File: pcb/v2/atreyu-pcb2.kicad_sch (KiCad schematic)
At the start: 126 parts, among them SW1 SW_Push, SW2 RotaryEncoder_Switch, SW3 RotaryEncoder_Switch, U1 Elite-C

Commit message: Checkpoint commit.
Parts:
- added J1: OLED, Connector_PinHeader_2.54mm:PinHeader_1x04_P2.54mm_Vertical, symbol SouffleKeyboard-rescue:OLED-Lily58-cache
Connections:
- net COL0: now also U1.26 (D5); no longer U1.8 (5/PC6)
- net COL1: now also U1.25 (B7); no longer U1.7 (4/PD4)
- net COL2: now also U1.8 (5/PC6); no longer U1.6 (3/PD0)
- net COL3: now also U1.7 (4/PD4); no longer U1.5 (2/PD1)
- net GND: now also J1.4 (P4)
- net VCC: now also J1.3 (P3)
- new net SCL: J1.2 (P2), U1.6 (3/PD0)
- new net SDA: J1.1 (P1), U1.5 (2/PD1)
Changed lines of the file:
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@@
+    )
+  )
+  (global_label "SCL" (shape input) (at 71.12 140.97 270) (fields_autoplaced)
+    (effects (font (size 1.27 1.27)) (justify right))
+    (property "Intersheet References" "${INTERSHEET_REFS}" (id 0) (at 71.0406 146.8907 90)
+      (effects (font (size 1.27 1.27)) (justify right) hide)
     )
   )
@@
     )
   )
+  (global_label "VCC" (shape input) (at 73.66 140.97 270) (fields_autoplaced)
+    (effects (font (size 1.27 1.27)) (justify right))
+    (property "Intersheet References" "${INTERSHEET_REFS}" (id 0) (at 73.5806 147.0117 90)
+      (effects (font (size 1.27 1.27)) (justify right) hide)
+    )
+  )
+  (global_label "SDA" (shape input) (at 96.52 158.75 180) (fields_autoplaced)
+    (effects (font (size 1.27 1.27)) (justify right))
+    (property "Intersheet References" "${INTERSHEET_REFS}" (id 0) (at 90.5388 158.6706 0)
+      (effects (font (size 1.27 1.27)) (justify right) hide)
+    )
+  )
   (global_label "SW54A" (shape input) (at 190.5 142.24 0) (fields_autoplaced)
     (effects (font (size 1.27 1.27)) (justify left))
@@
     )
   )
-  (global_label "COL3" (shape input) (at 96.52 158.75 180) (fields_autoplaced)
-    (effects (font (size 1.27 1.27)) (justify right))
-    (property "Intersheet References" "${INTERSHEET_REFS}" (id 0) (at 265.43 317.5 0)
+  (global_label "COL3" (shape input) (at 96.52 163.83 180) (fields_autoplaced)
+    (effects (font (size 1.27 1.27)) (justify right))
+    (property "Intersheet References" "${INTERSHEET_REFS}" (id 0) (at 265.43 322.58 0)
       (effects (font (size 1.27 1.27)) hide)
     )
@@
     )
   )
-  (global_label "COL0" (shape input) (at 96.52 166.37 180) (fields_autoplaced)
-    (effects (font (size 1.27 1.27)) (justify right))
-    (property "Intersheet References" "${INTERSHEET_REFS}" (id 0) (at -36.83 17.78 0)
-      (effects (font (size 1.27 1.27)) hide)
-    )
-  )
-  (global_label "COL2" (shape input) (at 96.52 161.29 180) (fields_autoplaced)
-    (effects (font (size 1.27 1.27)) (justify right))
-    (property "Intersheet References" "${INTERSHEET_REFS}" (id 0) (at -36.83 -2.54 0)
+  (global_label "SCL" (shape input) (at 96.52 161.29 180) (fields_autoplaced)
+    (effects (font (size 1.27 1.27)) (justify right))
+    (property "Intersheet References" "${INTERSHEET_REFS}" (id 0) (at 90.5993 161.2106 0)
+      (effects (font (size 1.27 1.27)) (justify right) hide)
+    )
+  )
+  (global_label "COL0" (shape input) (at 111.76 186.69 270) (fields_autoplaced)
+    (effects (font (size 1.27 1.27)) (justify right))
+    (property "Intersheet References" "${INTERSHEET_REFS}" (id 0) (at -36.83 320.04 0)
+      (effects (font (size 1.27 1.27)) hide)
+    )
+  )
+  (global_label "COL2" (shape input) (at 96.52 166.37 180) (fields_autoplaced)
+    (effects (font (size 1.27 1.27)) (justify right))
+    (property "Intersheet References" "${INTERSHEET_REFS}" (id 0) (at -36.83 2.54 0)
       (effects (font (size 1.27 1.27)) hide)
     )
@@
     )
   )
+  (global_label "SDA" (shape input) (at 68.58 140.97 270) (fields_autoplaced)
+    (effects (font (size 1.27 1.27)) (justify right))
+    (property "Intersheet References" "${INTERSHEET_REFS}" (id 0) (at 68.5006 146.9512 90)
+      (effects (font (size 1.27 1.27)) (justify right) hide)
+    )
+  )
   (global_label "COL5" (shape input) (at 96.52 148.59 180) (fields_autoplaced)
     (effects (font (size 1.27 1.27)) (justify right))
@@
     )
   )
-  (global_label "COL1" (shape input) (at 96.52 163.83 180) (fields_autoplaced)
-    (effects (font (size 1.27 1.27)) (justify right))
-    (property "Intersheet References" "${INTERSHEET_REFS}" (id 0) (at -36.83 12.7 0)
+  (global_label "COL1" (shape input) (at 109.22 186.69 270) (fields_autoplaced)
+    (effects (font (size 1.27 1.27)) (justify right))
+    (property "Intersheet References" "${INTERSHEET_REFS}" (id 0) (at -41.91 320.04 0)
       (effects (font (size 1.27 1.27)) hide)
     )
@@
     )
   )
+  (global_label "GND" (shape input) (at 76.2 140.97 270) (fields_autoplaced)
+    (effects (font (size 1.27 1.27)) (justify right))
+    (property "Intersheet References" "${INTERSHEET_REFS}" (id 0) (at 76.1206 147.2536 90)
+      (effects (font (size 1.27 1.27)) (justify right) hide)
+    )
+  )
   (global_label "COL3" (shape input) (at 85.09 26.67 90) (fields_autoplaced)
     (effects (font (size 1.27 1.27)) (justify left))
@@
     (pin "1")
     (pin "2")
+  )
+  (symbol (lib_id "SouffleKeyboard-rescue:OLED-Lily58-cache") (at 72.39 135.89 90) (unit 1)
+    (in_bom yes) (on_board yes)
+    (property "Reference" "J1" (id 0) (at 72.39 129.54 90))
+    (property "Value" "OLED" (id 1) (at 72.39 132.08 90))
+    (property "Footprint" "Connector_PinHeader_2.54mm:PinHeader_1x04_P2.54mm_Vertical" (id 2) (at 73.66 134.62 90)
+      (effects (font (size 1.27 1.27)) hide)
+    )
+    (property "Datasheet" "" (id 3) (at 72.39 135.89 0))
+    (pin "1")
+    (pin "2")
+    (pin "3")
+    (pin "4")
   )
   (symbol (lib_id "Device:D_Small") (at 238.76 91.44 90) (unit 1)
@@
       (reference "D60") (unit 1) (value "D_Small") (footprint "footprints:D3_hybrid_common_hole_connected_fix")
     )
+    (path "/1709f845-7847-4378-aef5-76eaf9944a35"
+      (reference "J1") (unit 1) (value "OLED") (footprint "Connector_PinHeader_2.54mm:PinHeader_1x04_P2.54mm_Vertical")
+    )
     (path "/8a1cdef1-da3d-41b0-8d52-3220205347ba"

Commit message: Checkpoint commit.
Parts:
- added J2: Conn_01x02_Female, Connector_PinHeader_2.54mm:PinHeader_1x02_P2.54mm_Vertical, symbol Connector:Conn_01x02_Female
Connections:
- net ENCC: now also U1.27 (C7); no longer U1.24 (B0)
- net GND: now also J2.2 (Pin_2)
- new net RAW: J2.1 (Pin_1), U1.24 (B0)
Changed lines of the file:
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@@
+    )
+  )
+  (global_label "GND" (shape input) (at 223.52 130.81 180) (fields_autoplaced)
+    (effects (font (size 1.27 1.27)) (justify right))
+    (property "Intersheet References" "${INTERSHEET_REFS}" (id 0) (at 217.2364 130.7306 0)
+      (effects (font (size 1.27 1.27)) (justify right) hide)
     )
   )
@@
     )
   )
+  (global_label "RAW" (shape input) (at 132.08 148.59 0) (fields_autoplaced)
+    (effects (font (size 1.27 1.27)) (justify left))
+    (property "Intersheet References" "${INTERSHEET_REFS}" (id 0) (at 138.3031 148.5106 0)
+      (effects (font (size 1.27 1.27)) (justify left) hide)
+    )
+  )
   (global_label "ROW4" (shape input) (at 132.08 176.53 0) (fields_autoplaced)
     (effects (font (size 1.27 1.27)) (justify left))
@@
     )
   )
-  (global_label "ENCC" (shape input) (at 132.08 148.59 0) (fields_autoplaced)
-    (effects (font (size 1.27 1.27)) (justify left))
-    (property "Intersheet References" "${INTERSHEET_REFS}" (id 0) (at 139.5126 148.6694 0)
-      (effects (font (size 1.27 1.27)) (justify left) hide)
-    )
-  )
   (global_label "COL4" (shape input) (at 99.06 26.67 90) (fields_autoplaced)
     (effects (font (size 1.27 1.27)) (justify left))
     (property "Intersheet References" "${INTERSHEET_REFS}" (id 0) (at 5.08 3.81 0)
       (effects (font (size 1.27 1.27)) hide)
+    )
+  )
+  (global_label "RAW" (shape input) (at 223.52 128.27 180) (fields_autoplaced)
+    (effects (font (size 1.27 1.27)) (justify right))
+    (property "Intersheet References" "${INTERSHEET_REFS}" (id 0) (at 217.2969 128.1906 0)
+      (effects (font (size 1.27 1.27)) (justify right) hide)
+    )
+  )
+  (global_label "ENCC" (shape input) (at 114.3 186.69 270) (fields_autoplaced)
+    (effects (font (size 1.27 1.27)) (justify right))
+    (property "Intersheet References" "${INTERSHEET_REFS}" (id 0) (at 114.2206 194.1226 90)
+      (effects (font (size 1.27 1.27)) (justify right) hide)
     )
   )
@@
     )
     (property "Datasheet" "~" (id 3) (at 252.73 91.44 90)
+      (effects (font (size 1.27 1.27)) hide)
+    )
+    (pin "1")
+    (pin "2")
+  )
+  (symbol (lib_id "Connector:Conn_01x02_Female") (at 228.6 128.27 0) (unit 1)
+    (in_bom yes) (on_board yes) (fields_autoplaced)
+    (property "Reference" "J2" (id 0) (at 229.87 128.2699 0)
+      (effects (font (size 1.27 1.27)) (justify left))
+    )
+    (property "Value" "Conn_01x02_Female" (id 1) (at 229.87 130.8099 0)
+      (effects (font (size 1.27 1.27)) (justify left))
+    )
+    (property "Footprint" "Connector_PinHeader_2.54mm:PinHeader_1x02_P2.54mm_Vertical" (id 2) (at 228.6 128.27 0)
+      (effects (font (size 1.27 1.27)) hide)
+    )
+    (property "Datasheet" "~" (id 3) (at 228.6 128.27 0)
       (effects (font (size 1.27 1.27)) hide)
     )
@@
       (reference "J1") (unit 1) (value "OLED") (footprint "Connector_PinHeader_2.54mm:PinHeader_1x04_P2.54mm_Vertical")
     )
+    (path "/328d0cfb-d3bb-449f-bae9-1be8568d8ed1"
+      (reference "J2") (unit 1) (value "Conn_01x02_Female") (footprint "Connector_PinHeader_2.54mm:PinHeader_1x02_P2.54mm_Vertical")
+    )
     (path "/8a1cdef1-da3d-41b0-8d52-3220205347ba"

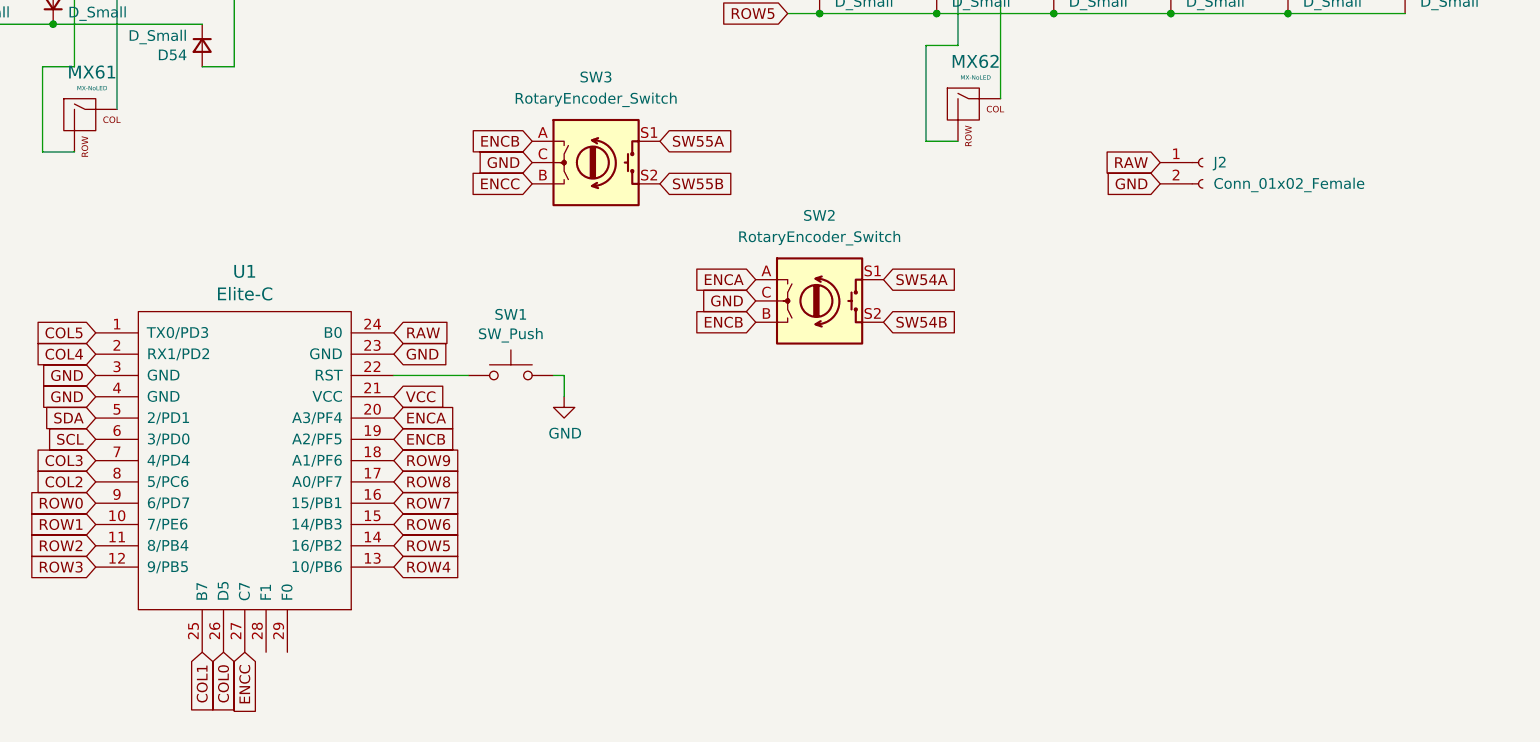
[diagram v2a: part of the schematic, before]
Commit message: Completed Nice!Nano and elite-c configurations.
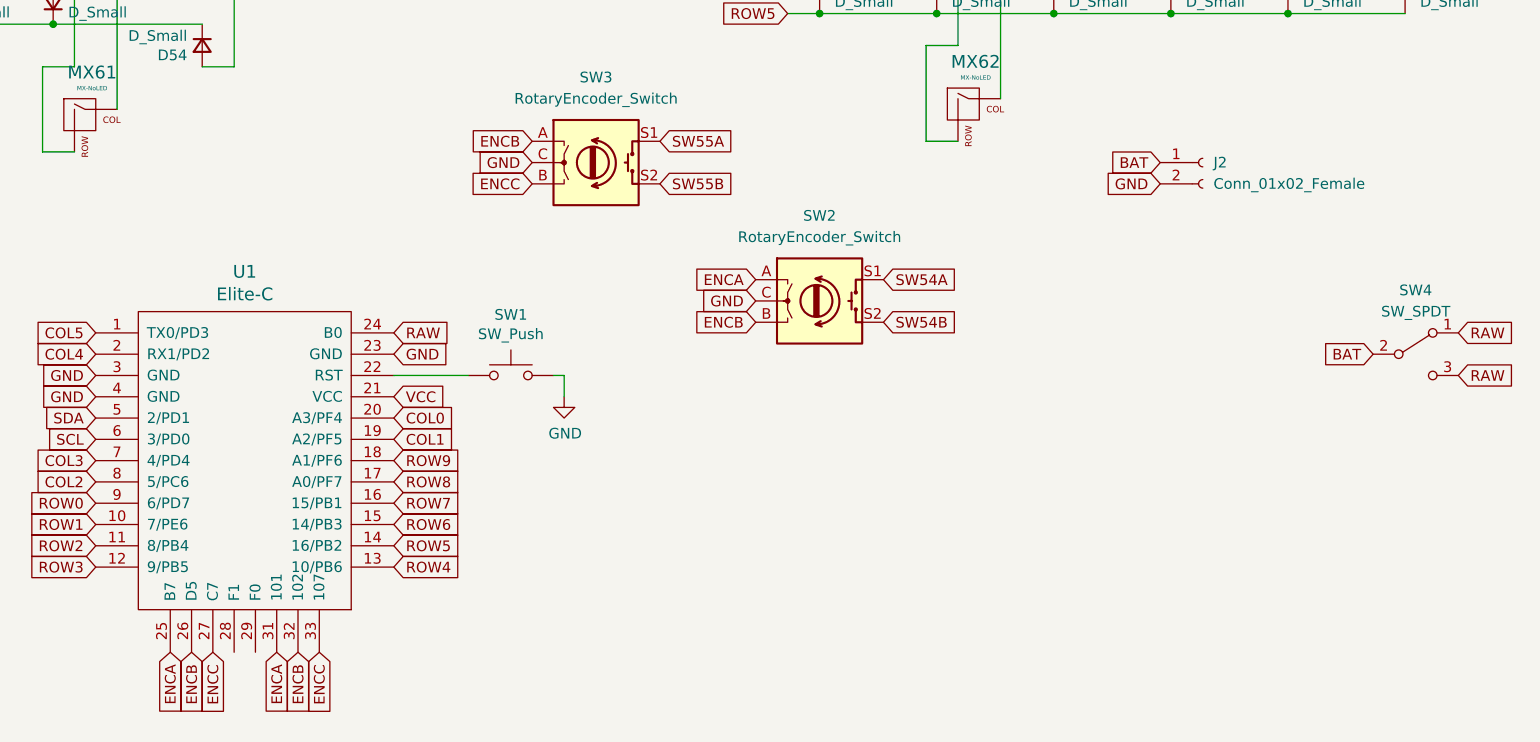
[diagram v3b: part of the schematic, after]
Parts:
- added SW4: SW_SPDT, footprints:Switch_MSK-12C01-07, symbol Switch:SW_SPDT
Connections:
- net COL0: now also U1.20 (A3/PF4); no longer U1.26 (D5)
- net COL1: now also U1.19 (A2/PF5); no longer U1.25 (B7)
- net ENCA: now also U1.25 (B7), U1.31 (101); no longer U1.20 (A3/PF4)
- net ENCB: now also U1.26 (D5), U1.32 (102); no longer U1.19 (A2/PF5)
- net ENCC: now also U1.33 (107)
- net RAW: now also SW4.1 (A), SW4.3 (C); no longer J2.1 (Pin_1)
- new net BAT: J2.1 (Pin_1), SW4.2 (B)
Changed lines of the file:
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@@
+    )
+  )
+  (global_label "ENCC" (shape input) (at 123.19 186.69 270) (fields_autoplaced)
+    (effects (font (size 1.27 1.27)) (justify right))
+    (property "Intersheet References" "${INTERSHEET_REFS}" (id 0) (at 123.1106 194.1226 90)
+      (effects (font (size 1.27 1.27)) (justify right) hide)
     )
   )
@@
     )
   )
-  (global_label "ENCB" (shape input) (at 132.08 161.29 0) (fields_autoplaced)
-    (effects (font (size 1.27 1.27)) (justify left))
-    (property "Intersheet References" "${INTERSHEET_REFS}" (id 0) (at 139.5126 161.2106 0)
+  (global_label "COL1" (shape input) (at 132.08 161.29 0) (fields_autoplaced)
+    (effects (font (size 1.27 1.27)) (justify left))
+    (property "Intersheet References" "${INTERSHEET_REFS}" (id 0) (at 139.3312 161.2106 0)
       (effects (font (size 1.27 1.27)) (justify left) hide)
     )
   )
-  (global_label "ENCA" (shape input) (at 132.08 158.75 0) (fields_autoplaced)
+  (global_label "COL0" (shape input) (at 132.08 158.75 0) (fields_autoplaced)
     (effects (font (size 1.27 1.27)) (justify left))
     (property "Intersheet References" "${INTERSHEET_REFS}" (id 0) (at 139.3312 158.6706 0)
@@
     )
   )
+  (global_label "RAW" (shape input) (at 259.08 153.67 0) (fields_autoplaced)
+    (effects (font (size 1.27 1.27)) (justify left))
+    (property "Intersheet References" "${INTERSHEET_REFS}" (id 0) (at 265.3031 153.7494 0)
+      (effects (font (size 1.27 1.27)) (justify left) hide)
+    )
+  )
   (global_label "COL5" (shape input) (at 190.5 25.4 90) (fields_autoplaced)
     (effects (font (size 1.27 1.27)) (justify left))
@@
     )
   )
+  (global_label "BAT" (shape input) (at 248.92 151.13 180) (fields_autoplaced)
+    (effects (font (size 1.27 1.27)) (justify right))
+    (property "Intersheet References" "${INTERSHEET_REFS}" (id 0) (at 243.1807 151.2094 0)
+      (effects (font (size 1.27 1.27)) (justify right) hide)
+    )
+  )
   (global_label "ROW1" (shape input) (at 31.75 62.23 180) (fields_autoplaced)
     (effects (font (size 1.27 1.27)) (justify right))
     (property "Intersheet References" "${INTERSHEET_REFS}" (id 0) (at 5.08 3.81 0)
       (effects (font (size 1.27 1.27)) hide)
+    )
+  )
+  (global_label "BAT" (shape input) (at 223.52 128.27 180) (fields_autoplaced)
+    (effects (font (size 1.27 1.27)) (justify right))
+    (property "Intersheet References" "${INTERSHEET_REFS}" (id 0) (at 217.7807 128.3494 0)
+      (effects (font (size 1.27 1.27)) (justify right) hide)
     )
   )
@@
     )
   )
+  (global_label "RAW" (shape input) (at 259.08 148.59 0) (fields_autoplaced)
+    (effects (font (size 1.27 1.27)) (justify left))
+    (property "Intersheet References" "${INTERSHEET_REFS}" (id 0) (at 265.3031 148.6694 0)
+      (effects (font (size 1.27 1.27)) (justify left) hide)
+    )
+  )
   (global_label "RAW" (shape input) (at 132.08 148.59 0) (fields_autoplaced)
     (effects (font (size 1.27 1.27)) (justify left))
@@
     )
   )
-  (global_label "RAW" (shape input) (at 223.52 128.27 180) (fields_autoplaced)
-    (effects (font (size 1.27 1.27)) (justify right))
-    (property "Intersheet References" "${INTERSHEET_REFS}" (id 0) (at 217.2969 128.1906 0)
+  (global_label "ENCA" (shape input) (at 118.11 186.69 270) (fields_autoplaced)
+    (effects (font (size 1.27 1.27)) (justify right))
+    (property "Intersheet References" "${INTERSHEET_REFS}" (id 0) (at 118.0306 193.9412 90)
       (effects (font (size 1.27 1.27)) (justify right) hide)
     )
   )
-  (global_label "ENCC" (shape input) (at 114.3 186.69 270) (fields_autoplaced)
-    (effects (font (size 1.27 1.27)) (justify right))
-    (property "Intersheet References" "${INTERSHEET_REFS}" (id 0) (at 114.2206 194.1226 90)
+  (global_label "ENCB" (shape input) (at 120.65 186.69 270) (fields_autoplaced)
+    (effects (font (size 1.27 1.27)) (justify right))
+    (property "Intersheet References" "${INTERSHEET_REFS}" (id 0) (at 120.5706 194.1226 90)
+      (effects (font (size 1.27 1.27)) (justify right) hide)
+    )
+  )
+  (global_label "ENCC" (shape input) (at 110.49 186.69 270) (fields_autoplaced)
+    (effects (font (size 1.27 1.27)) (justify right))
+    (property "Intersheet References" "${INTERSHEET_REFS}" (id 0) (at 110.4106 194.1226 90)
       (effects (font (size 1.27 1.27)) (justify right) hide)
     )
@@
     )
   )
-  (global_label "COL0" (shape input) (at 111.76 186.69 270) (fields_autoplaced)
-    (effects (font (size 1.27 1.27)) (justify right))
-    (property "Intersheet References" "${INTERSHEET_REFS}" (id 0) (at -36.83 320.04 0)
-      (effects (font (size 1.27 1.27)) hide)
+  (global_label "ENCB" (shape input) (at 107.95 186.69 270) (fields_autoplaced)
+    (effects (font (size 1.27 1.27)) (justify right))
+    (property "Intersheet References" "${INTERSHEET_REFS}" (id 0) (at 107.8706 194.1226 90)
+      (effects (font (size 1.27 1.27)) (justify right) hide)
     )
   )
@@
     )
   )
-  (global_label "COL1" (shape input) (at 109.22 186.69 270) (fields_autoplaced)
-    (effects (font (size 1.27 1.27)) (justify right))
-    (property "Intersheet References" "${INTERSHEET_REFS}" (id 0) (at -41.91 320.04 0)
-      (effects (font (size 1.27 1.27)) hide)
+  (global_label "ENCA" (shape input) (at 105.41 186.69 270) (fields_autoplaced)
+    (effects (font (size 1.27 1.27)) (justify right))
+    (property "Intersheet References" "${INTERSHEET_REFS}" (id 0) (at 105.3306 193.9412 90)
+      (effects (font (size 1.27 1.27)) (justify right) hide)
     )
   )
@@
     (pin "29")
     (pin "3")
+    (pin "31")
+    (pin "32")
+    (pin "33")
     (pin "4")
     (pin "5")
@@
     (pin "2")
   )
+  (symbol (lib_id "Switch:SW_SPDT") (at 254 151.13 0) (unit 1)
+    (in_bom yes) (on_board yes) (fields_autoplaced)
+    (property "Reference" "SW4" (id 0) (at 254 143.51 0))
+    (property "Value" "SW_SPDT" (id 1) (at 254 146.05 0))
+    (property "Footprint" "footprints:Switch_MSK-12C01-07" (id 2) (at 254 151.13 0)
+      (effects (font (size 1.27 1.27)) hide)
+    )
+    (property "Datasheet" "~" (id 3) (at 254 151.13 0)
+      (effects (font (size 1.27 1.27)) hide)
+    )
+    (pin "1")
+    (pin "2")
+    (pin "3")
+  )
   (symbol (lib_id "MX_Alps_Hybrid:MX-NoLED") (at 81.28 69.85 0) (unit 1)
     (in_bom yes) (on_board yes)
@@
       (reference "SW3") (unit 1) (value "RotaryEncoder_Switch") (footprint "footprints:RotaryEncoder_EC11")
     )
+    (path "/9ce24d3f-ec81-4be1-9c99-1bd29e5f7113"
+      (reference "SW4") (unit 1) (value "SW_SPDT") (footprint "footprints:Switch_MSK-12C01-07")
+    )
     (path "/55d3bb9a-fd07-47f6-ac8c-0b322236c705"
